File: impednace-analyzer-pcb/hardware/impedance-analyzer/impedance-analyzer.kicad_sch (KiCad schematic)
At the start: 17 parts, among them J1 AD9833, J10 Conn_01x08, J11 Conn_01x08, J12 Conn_01x08, J2 ADS1256_SPI, J3 ADS1256_AIN, J4 UNO_POWER, J5 UNO_ANALOG, J6 UNO_DIGITAL_LOW, J7 UNO_DIGITAL_HIGH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

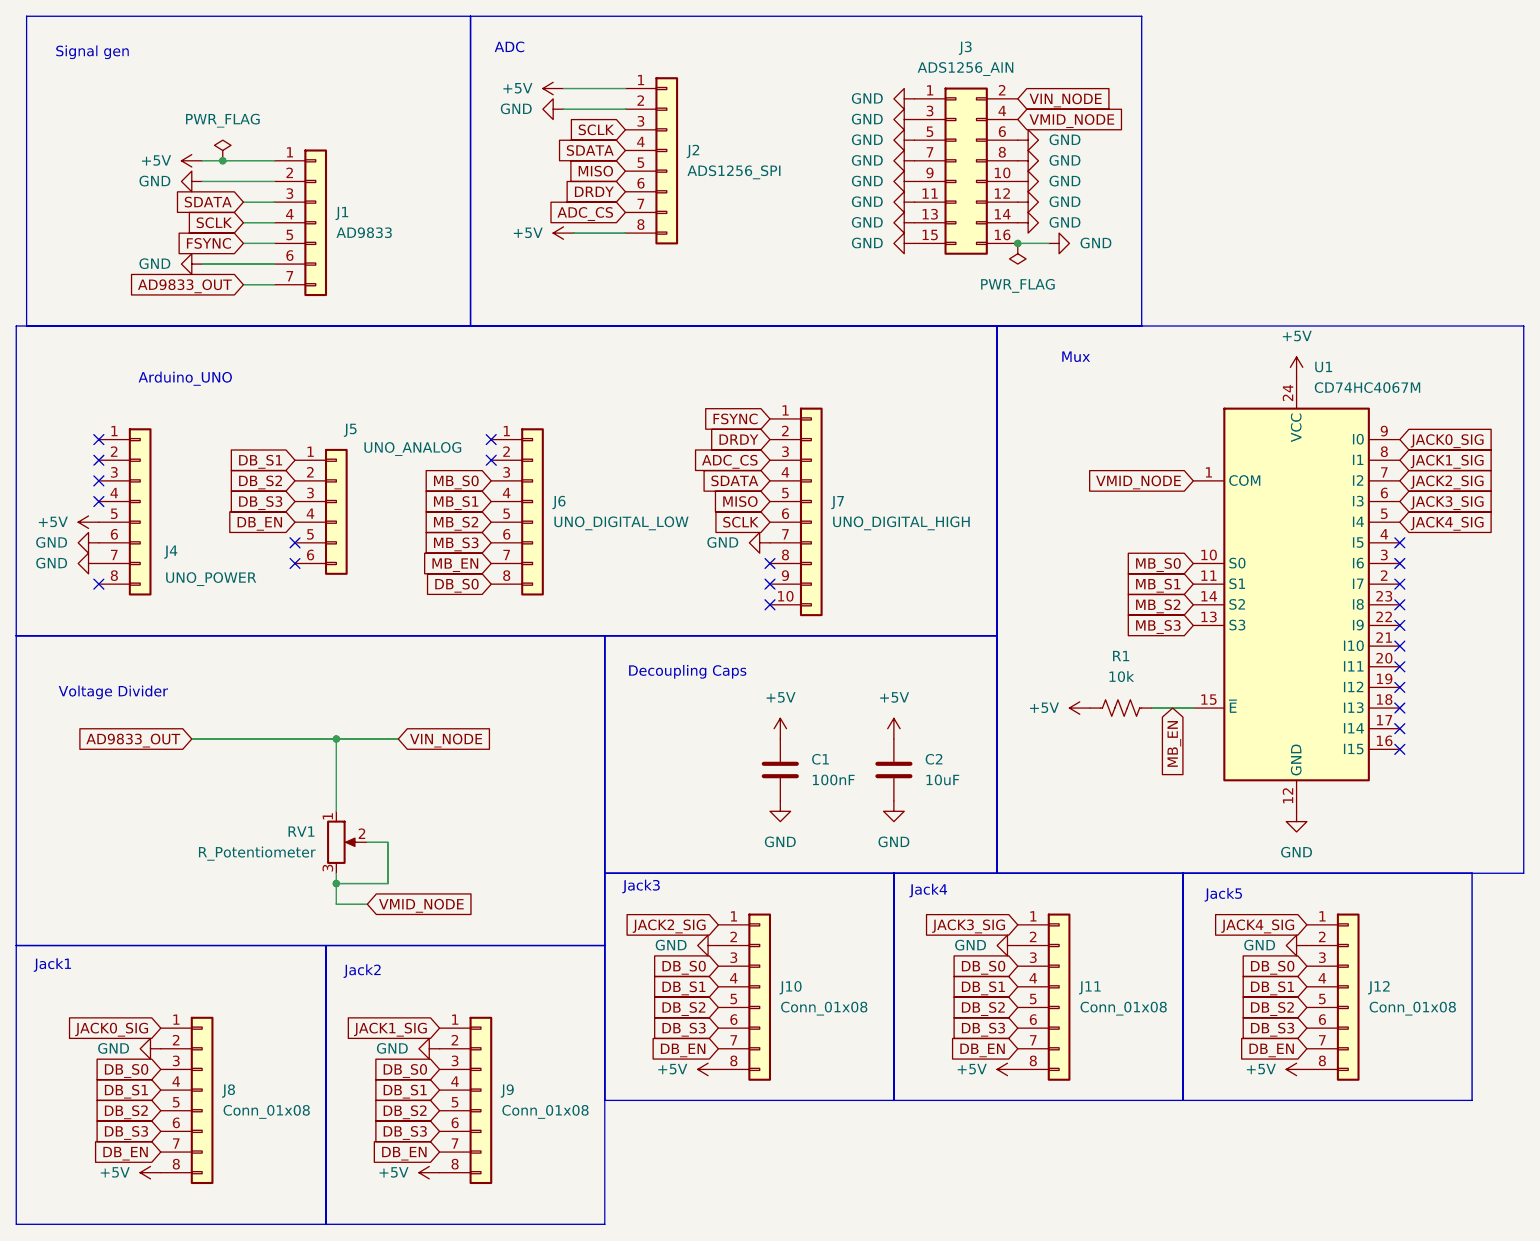
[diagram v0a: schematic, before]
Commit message: finished placement and started routing
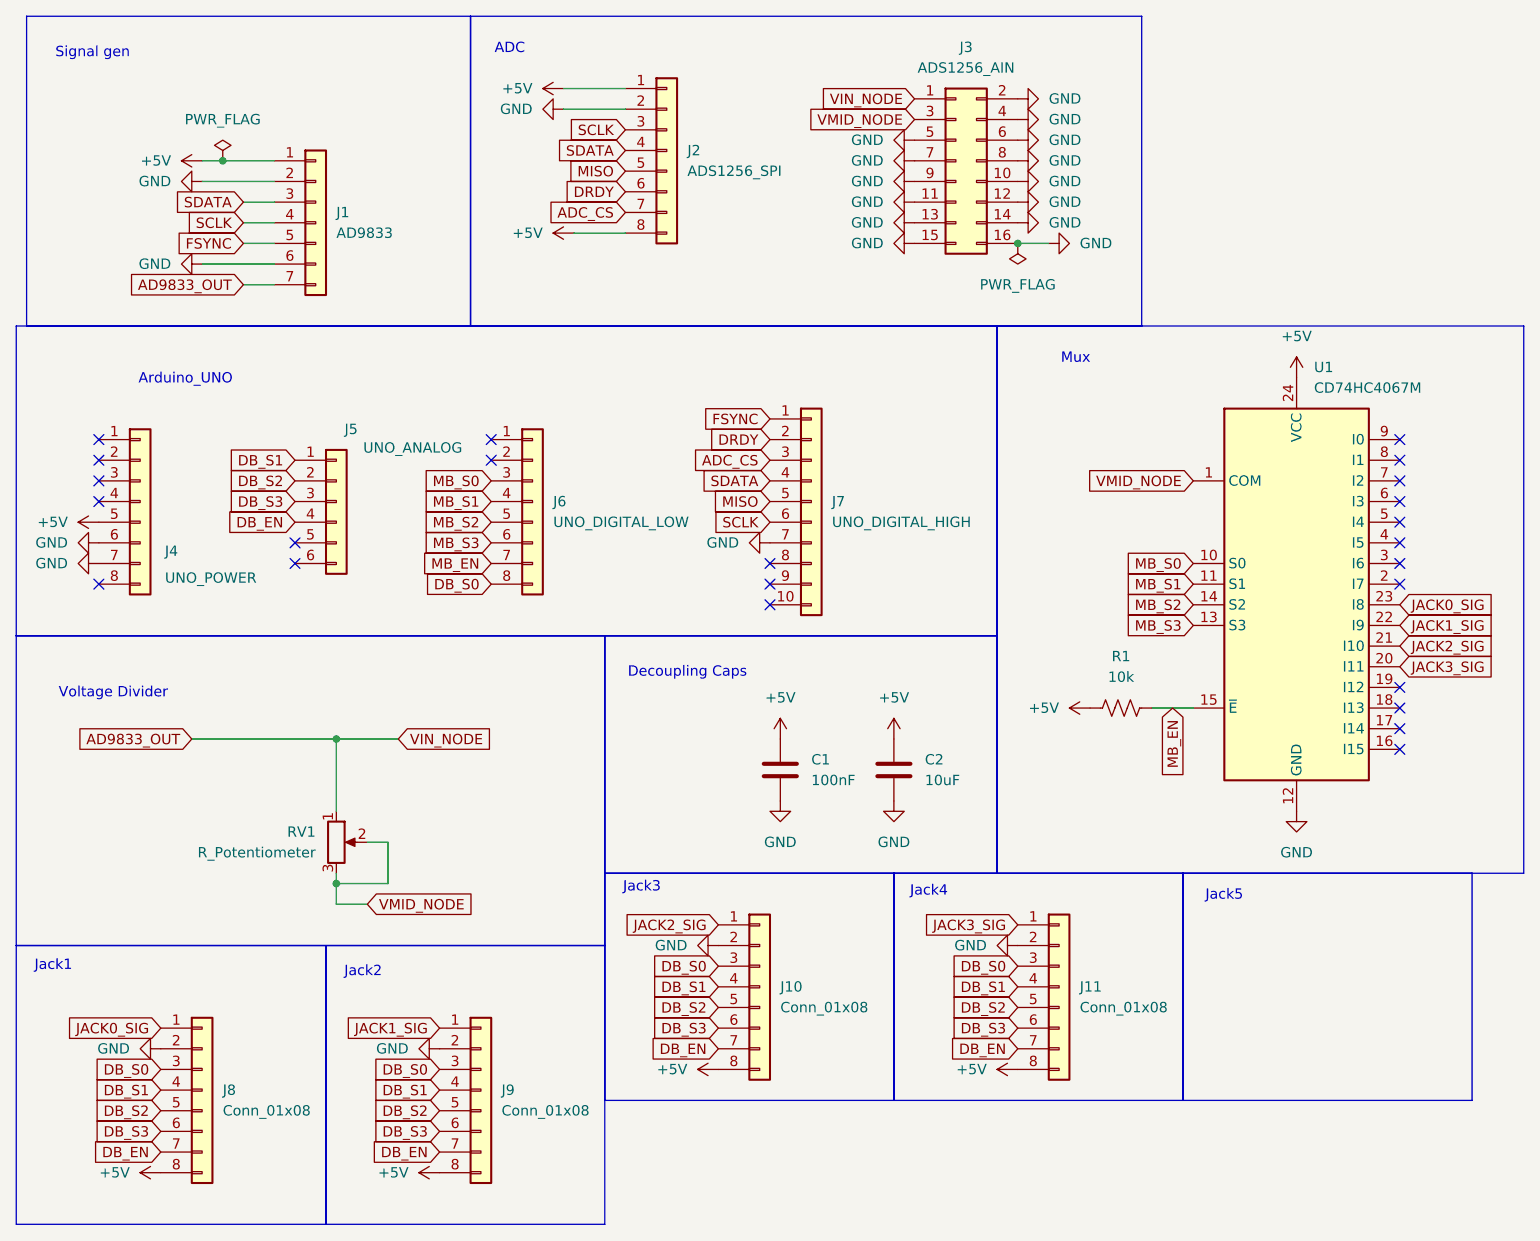
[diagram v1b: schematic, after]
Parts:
- removed J12: Conn_01x08, Connector_Molex:Molex_Micro-Fit_3.0_43650-0815_1x08_P3.00mm_Vertical, symbol Connector_Generic:Conn_01x08
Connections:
- net AD9833_OUT: now also J3.1 (Pin_1); no longer J3.2 (Pin_2)
- net GND: now also J3.2 (Pin_2), J3.4 (Pin_4); no longer J3.1 (Pin_1), J3.3 (Pin_3)
- net JACK0_SIG: now also U1.23 (I8); no longer U1.9 (I0)
- net JACK1_SIG: now also U1.22 (I9); no longer U1.8 (I1)
- net JACK2_SIG: now also U1.21 (I10); no longer U1.7 (I2)
- net JACK3_SIG: now also U1.20 (I11); no longer U1.6 (I3)
- net VMID_NODE: now also J3.3 (Pin_3); no longer J3.4 (Pin_4)
- net JACK4_SIG: no longer names the net of U1.5 (I4)
- no-connect marks 23 -> 24
